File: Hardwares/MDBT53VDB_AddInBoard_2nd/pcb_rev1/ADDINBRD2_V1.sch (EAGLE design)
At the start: 11 parts, among them Q1 DMP2035UFDF-7, Q2 BC817-40QA, SW1 SKRPACE010, U1 SN74AHC1G00DRLR, U2 REF3325AIRSER

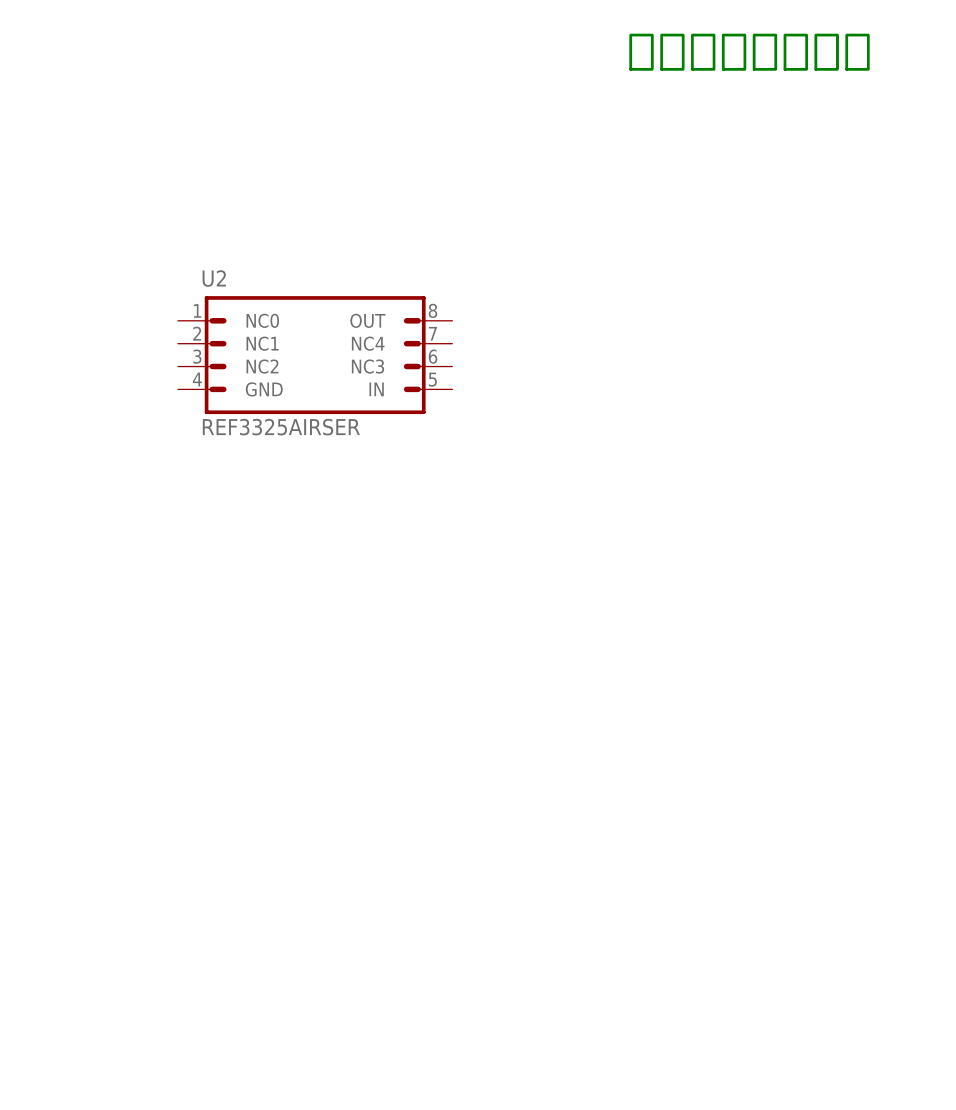
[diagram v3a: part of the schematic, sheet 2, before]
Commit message: 回路図を修正
・基準電圧回路にバイパスコンデンサーを配置
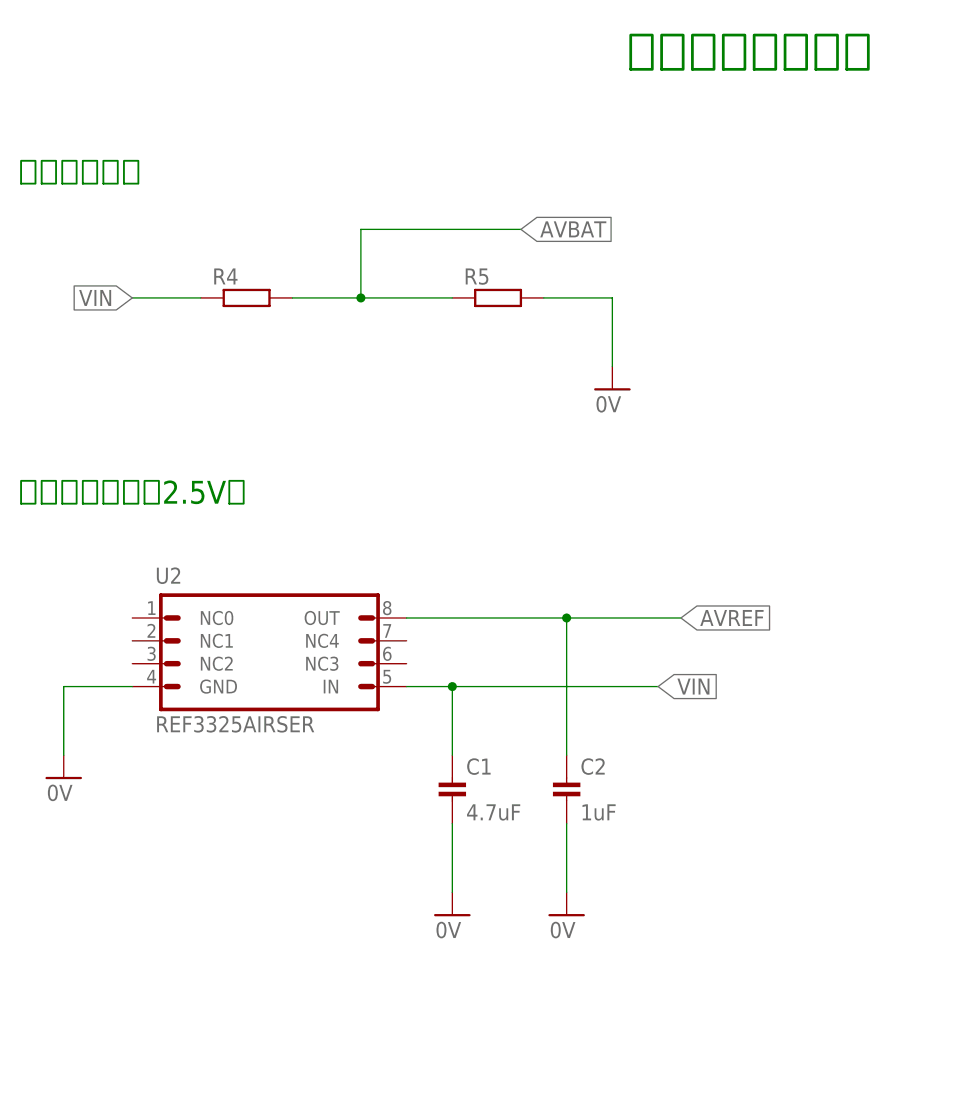
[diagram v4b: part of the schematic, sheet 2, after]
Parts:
- added C1: 4.7uF, SMDs:JMK105BBJ475MVHF
- added C2: 1uF, SMDs:GRM155R70J105KA12J
- added R4, R5: (no value), Parts:RESISTOR_0402N
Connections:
- new net AVBAT: R4.2, R5.1
- new net AVREF: C2.1, U2.OUT
- net 0V: now also C1.2, C2.2, R5.2, U2.GND
- net VIN: now also C1.1, R4.1, U2.IN
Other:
- note added: "基準電圧生成（2.5V）"
- note added: "電源電圧分圧"
- moved on the sheet: U2
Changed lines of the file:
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@@
 <part name="GND4" library="Supply" deviceset="0V" device=""/>
 <part name="U2" library="ICs" deviceset="REF33" device="25AIRSER"/>
+<part name="R4" library="Parts" deviceset="RESISTOR" device="_0402N"/>
+<part name="R5" library="Parts" deviceset="RESISTOR" device="_0402N"/>
+<part name="GND5" library="Supply" deviceset="0V" device=""/>
+<part name="GND6" library="Supply" deviceset="0V" device=""/>
+<part name="GND7" library="Supply" deviceset="0V" device=""/>
+<part name="GND8" library="Supply" deviceset="0V" device=""/>
+<part name="C1" library="SMDs" deviceset="JMK105BBJ" device="475MVHF" value="4.7uF"/>
+<part name="C2" library="SMDs" deviceset="GRM155" device="R70J105KA12J" value="1uF"/>
 </parts>
 <sheets>
@@
 for MDBT53V-DB</text>
 <text x="129.54" y="152.4" size="3.81" layer="91" align="bottom-center">電源電圧測定回路</text>
+<text x="48.26" y="142.24" size="2.54" layer="91" align="top-left">電源電圧分圧</text>
+<text x="48.26" y="106.68" size="2.54" layer="91" align="top-left">基準電圧生成（2.5V）</text>
 </plain>
 <instances>
 <instance part="FRAME2" gate="G$1" x="0" y="0"/>
-<instance part="U2" gate="G$1" x="81.28" y="119.38"/>
+<instance part="U2" gate="G$1" x="76.2" y="86.36"/>
+<instance part="R4" gate="G$1" x="68.58" y="127"/>
+<instance part="R5" gate="G$1" x="96.52" y="127"/>
+<instance part="GND5" gate="1" x="114.3" y="116.84"/>
+<instance part="GND6" gate="1" x="53.34" y="73.66"/>
+<instance part="GND7" gate="1" x="96.52" y="58.42"/>
+<instance part="GND8" gate="1" x="109.22" y="58.42"/>
+<instance part="C1" gate="G$1" x="96.52" y="76.2"/>
+<instance part="C2" gate="G$1" x="109.22" y="76.2"/>
 </instances>
 <busses>
 </busses>
 <nets>
+<net name="VIN" class="0">
+<segment>
+<pinref part="R4" gate="G$1" pin="1"/>
+<wire x1="68.58" y1="127" x2="60.96" y2="127" width="0.1524" layer="91"/>
+<label x="60.96" y="127" size="1.778" layer="95" rot="R180" xref="yes"/>
+</segment>
+<segment>
+<pinref part="U2" gate="G$1" pin="IN"/>
+<wire x1="91.44" y1="83.82" x2="96.52" y2="83.82" width="0.1524" layer="91"/>
+<label x="119.38" y="83.82" size="1.778" layer="95" xref="yes"/>
+<wire x1="96.52" y1="83.82" x2="119.38" y2="83.82" width="0.1524" layer="91"/>
+<junction x="96.52" y="83.82"/>
+<pinref part="C1" gate="G$1" pin="1"/>
+<wire x1="96.52" y1="83.82" x2="96.52" y2="76.2" width="0.1524" layer="91"/>
+</segment>
+</net>
+<net name="AVBAT" class="0">
+<segment>
+<pinref part="R4" gate="G$1" pin="2"/>
+<pinref part="R5" gate="G$1" pin="1"/>
+<wire x1="78.74" y1="127" x2="86.36" y2="127" width="0.1524" layer="91"/>
+<wire x1="86.36" y1="127" x2="96.52" y2="127" width="0.1524" layer="91"/>
+<wire x1="86.36" y1="127" x2="86.36" y2="134.62" width="0.1524" layer="91"/>
+<wire x1="86.36" y1="134.62" x2="104.14" y2="134.62" width="0.1524" layer="91"/>
+<junction x="86.36" y="127"/>
+<label x="104.14" y="134.62" size="1.778" layer="95" xref="yes"/>
+</segment>
+</net>
+<net name="0V" class="0">
+<segment>
+<pinref part="R5" gate="G$1" pin="2"/>
+<pinref part="GND5" gate="1" pin="0V"/>
+<wire x1="106.68" y1="127" x2="114.3" y2="127" width="0.1524" layer="91"/>
+<wire x1="114.3" y1="127" x2="114.3" y2="119.38" width="0.1524" layer="91"/>
+</segment>
+<segment>
+<pinref part="U2" gate="G$1" pin="GND"/>
+<pinref part="GND6" gate="1" pin="0V"/>
+<wire x1="60.96" y1="83.82" x2="53.34" y2="83.82" width="0.1524" layer="91"/>
+<wire x1="53.34" y1="83.82" x2="53.34" y2="76.2" width="0.1524" layer="91"/>
+</segment>
+<segment>
+<pinref part="C1" gate="G$1" pin="2"/>
+<pinref part="GND7" gate="1" pin="0V"/>
+<wire x1="96.52" y1="68.58" x2="96.52" y2="60.96" width="0.1524" layer="91"/>
+</segment>
+<segment>
+<pinref part="C2" gate="G$1" pin="2"/>
+<pinref part="GND8" gate="1" pin="0V"/>
+<wire x1="109.22" y1="68.58" x2="109.22" y2="60.96" width="0.1524" layer="91"/>
+</segment>
+</net>
+<net name="AVREF" class="0">
+<segment>
+<pinref part="U2" gate="G$1" pin="OUT"/>
+<wire x1="91.44" y1="91.44" x2="109.22" y2="91.44" width="0.1524" layer="91"/>
+<label x="121.92" y="91.44" size="1.778" layer="95" xref="yes"/>
+<wire x1="109.22" y1="91.44" x2="121.92" y2="91.44" width="0.1524" layer="91"/>
+<junction x="109.22" y="91.44"/>
+<pinref part="C2" gate="G$1" pin="1"/>
+<wire x1="109.22" y1="91.44" x2="109.22" y2="76.2" width="0.1524" layer="91"/>
+</segment>
+</net>
 </nets>
 </sheet>

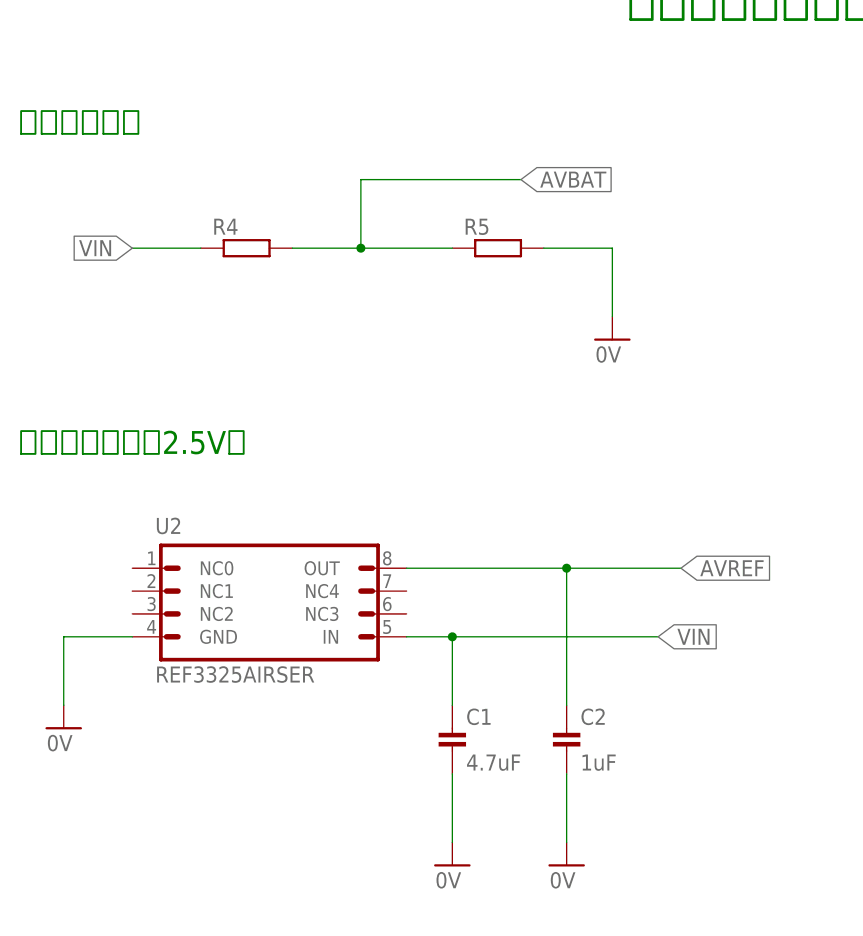
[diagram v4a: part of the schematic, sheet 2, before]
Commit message: 回路図を修正
・分圧回路を追加
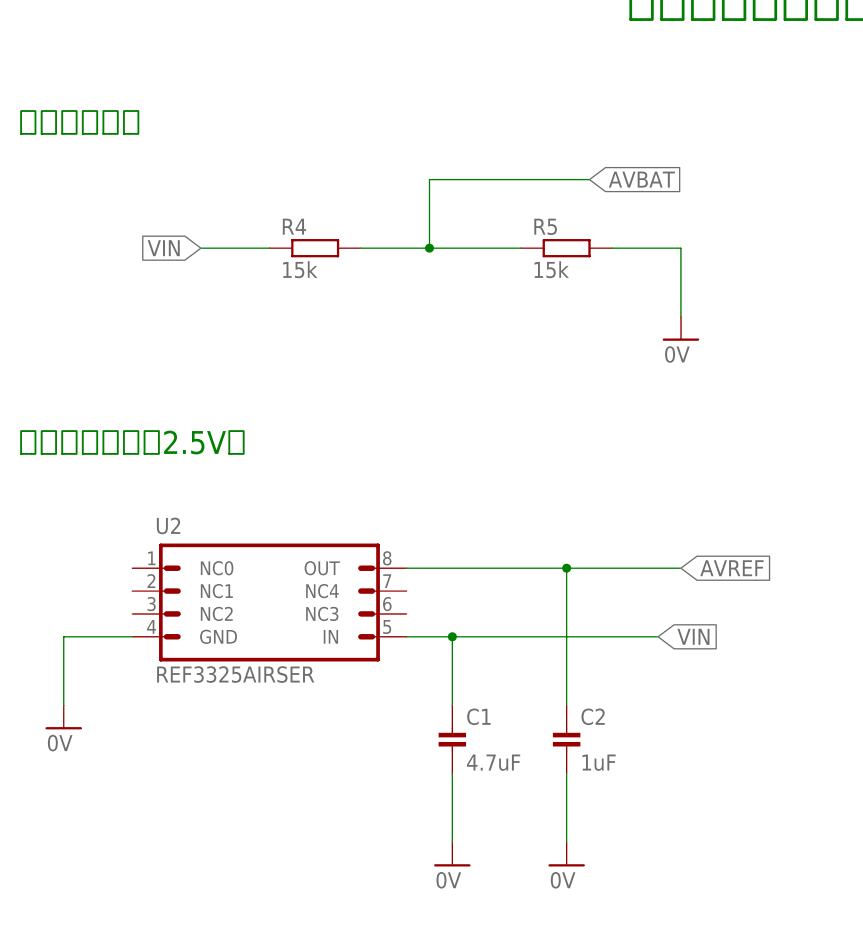
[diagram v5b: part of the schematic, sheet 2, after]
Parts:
- R4, R5: value (none) -> 15k; device Parts:RESISTOR_0402N -> SMDs:ERA-2APB153X
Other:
- moved on the sheet: R4, R5
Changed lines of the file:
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@@
 <part name="GND4" library="Supply" deviceset="0V" device=""/>
 <part name="U2" library="ICs" deviceset="REF33" device="25AIRSER"/>
-<part name="R4" library="Parts" deviceset="RESISTOR" device="_0402N"/>
-<part name="R5" library="Parts" deviceset="RESISTOR" device="_0402N"/>
 <part name="GND5" library="Supply" deviceset="0V" device=""/>
 <part name="GND6" library="Supply" deviceset="0V" device=""/>
@@
 <part name="C1" library="SMDs" deviceset="JMK105BBJ" device="475MVHF" value="4.7uF"/>
 <part name="C2" library="SMDs" deviceset="GRM155" device="R70J105KA12J" value="1uF"/>
+<part name="R4" library="SMDs" deviceset="ERA-2A" device="PB153X" value="15k"/>
+<part name="R5" library="SMDs" deviceset="ERA-2A" device="PB153X" value="15k"/>
 </parts>
 <sheets>
@@
 <instance part="FRAME2" gate="G$1" x="0" y="0"/>
 <instance part="U2" gate="G$1" x="76.2" y="86.36"/>
-<instance part="R4" gate="G$1" x="68.58" y="127"/>
-<instance part="R5" gate="G$1" x="96.52" y="127"/>
-<instance part="GND5" gate="1" x="114.3" y="116.84"/>
+<instance part="GND5" gate="1" x="121.92" y="116.84"/>
 <instance part="GND6" gate="1" x="53.34" y="73.66"/>
 <instance part="GND7" gate="1" x="96.52" y="58.42"/>
 <instance part="GND8" gate="1" x="109.22" y="58.42"/>
-<instance part="C1" gate="G$1" x="96.52" y="76.2"/>
-<instance part="C2" gate="G$1" x="109.22" y="76.2"/>
+<instance part="C1" gate="G$1" x="96.52" y="73.66"/>
+<instance part="C2" gate="G$1" x="109.22" y="73.66"/>
+<instance part="R4" gate="G$1" x="81.28" y="127"/>
+<instance part="R5" gate="G$1" x="109.22" y="127"/>
 </instances>
 <busses>
@@
 <net name="VIN" class="0">
 <segment>
+<wire x1="76.2" y1="127" x2="68.58" y2="127" width="0.1524" layer="91"/>
+<label x="68.58" y="127" size="1.778" layer="95" rot="R180" xref="yes"/>
 <pinref part="R4" gate="G$1" pin="1"/>
-<wire x1="68.58" y1="127" x2="60.96" y2="127" width="0.1524" layer="91"/>
-<label x="60.96" y="127" size="1.778" layer="95" rot="R180" xref="yes"/>
 </segment>
 <segment>
@@
 <net name="AVBAT" class="0">
 <segment>
+<wire x1="86.36" y1="127" x2="93.98" y2="127" width="0.1524" layer="91"/>
+<wire x1="93.98" y1="127" x2="104.14" y2="127" width="0.1524" layer="91"/>
+<wire x1="93.98" y1="127" x2="93.98" y2="134.62" width="0.1524" layer="91"/>
+<wire x1="93.98" y1="134.62" x2="111.76" y2="134.62" width="0.1524" layer="91"/>
+<junction x="93.98" y="127"/>
+<label x="111.76" y="134.62" size="1.778" layer="95" xref="yes"/>
 <pinref part="R4" gate="G$1" pin="2"/>
 <pinref part="R5" gate="G$1" pin="1"/>
-<wire x1="78.74" y1="127" x2="86.36" y2="127" width="0.1524" layer="91"/>
-<wire x1="86.36" y1="127" x2="96.52" y2="127" width="0.1524" layer="91"/>
-<wire x1="86.36" y1="127" x2="86.36" y2="134.62" width="0.1524" layer="91"/>
-<wire x1="86.36" y1="134.62" x2="104.14" y2="134.62" width="0.1524" layer="91"/>
-<junction x="86.36" y="127"/>
-<label x="104.14" y="134.62" size="1.778" layer="95" xref="yes"/>
 </segment>
 </net>
 <net name="0V" class="0">
 <segment>
+<pinref part="GND5" gate="1" pin="0V"/>
+<wire x1="114.3" y1="127" x2="121.92" y2="127" width="0.1524" layer="91"/>
+<wire x1="121.92" y1="127" x2="121.92" y2="119.38" width="0.1524" layer="91"/>
 <pinref part="R5" gate="G$1" pin="2"/>
-<pinref part="GND5" gate="1" pin="0V"/>
-<wire x1="106.68" y1="127" x2="114.3" y2="127" width="0.1524" layer="91"/>
-<wire x1="114.3" y1="127" x2="114.3" y2="119.38" width="0.1524" layer="91"/>
-</segment>
-<segment>
+</segment>
+<segment>

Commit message: レイアウトを修正
・シルクの位置を修正
・部品ライブラリーの一部を入れ替え
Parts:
- F1: device Parts:FCC16102ABTP -> SMDs:FCC16102ABTP
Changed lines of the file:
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@@
 <part name="FRAME1" library="Generic" deviceset="A4L-LOC" device=""/>
 <part name="FRAME2" library="Generic" deviceset="A4L-LOC" device=""/>
-<part name="F1" library="Parts" deviceset="FCC16" device="102ABTP"/>
+<part name="F1" library="SMDs" deviceset="FCC16" device="102ABTP"/>
 <part name="D1" library="Parts" deviceset="PMEG4010" device="AESBYL"/>
 <part name="SW1" library="Parts" deviceset="SKRPACE010" device=""/>

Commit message: レイアウトを修正
・部品ライブラリーの一部を入れ替え
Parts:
- R1, R2: device Parts:RESISTOR_0402N -> SMDs:CRCW04025K10FKEDC
- R3: device Parts:RESISTOR_0402N -> SMDs:CRCW040251K0FKEDC
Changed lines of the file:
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@@
 <part name="GND1" library="Supply" deviceset="0V" device=""/>
 <part name="GND2" library="Supply" deviceset="0V" device=""/>
-<part name="R1" library="Parts" deviceset="RESISTOR" device="_0402N" value="5.1k"/>
+<part name="R1" library="SMDs" deviceset="CRCW0402" device="5K10FKEDC" value="5.1k"/>
 <part name="D2" library="Parts" deviceset="PMEG4010" device="AESBYL"/>
 <part name="Q1" library="Parts" deviceset="DMP2035" device="UFDF-7"/>
@@
 <part name="Q2" library="Parts" deviceset="BC817" device="-40QA"/>
 <part name="GND3" library="Supply" deviceset="0V" device=""/>
-<part name="R2" library="Parts" deviceset="RESISTOR" device="_0402N" value="5.1k"/>
-<part name="R3" library="Parts" deviceset="RESISTOR" device="_0402N" value="51k"/>
+<part name="R2" library="SMDs" deviceset="CRCW0402" device="5K10FKEDC" value="5.1k"/>
+<part name="R3" library="SMDs" deviceset="CRCW0402" device="51K0FKEDC" value="51k"/>
 <part name="GND4" library="Supply" deviceset="0V" device=""/>
 <part name="U2" library="ICs" deviceset="REF33" device="25AIRSER"/>
@@
 <instance part="GND1" gate="1" x="116.84" y="116.84"/>
 <instance part="GND2" gate="1" x="132.08" y="88.9"/>
-<instance part="R1" gate="G$1" x="132.08" y="121.92" rot="R90"/>
+<instance part="R1" gate="G$1" x="132.08" y="127" rot="R90"/>
 <instance part="D2" gate="G$1" x="170.18" y="137.16" smashed="yes">
 <attribute name="NAME" x="162.56" y="132.08" size="1.778" layer="95"/>
@@
 <instance part="Q2" gate="G$1" x="162.56" y="63.5"/>
 <instance part="GND3" gate="1" x="101.6" y="50.8"/>
-<instance part="R2" gate="G$1" x="142.24" y="63.5"/>
-<instance part="R3" gate="G$1" x="157.48" y="48.26" rot="R90"/>
+<instance part="R2" gate="G$1" x="147.32" y="63.5"/>
+<instance part="R3" gate="G$1" x="157.48" y="53.34" rot="R90"/>
 <instance part="GND4" gate="1" x="167.64" y="35.56"/>
 </instances>
@@
 <pinref part="F1" gate="G$1" pin="2"/>
 <wire x1="99.06" y1="137.16" x2="116.84" y2="137.16" width="0.1524" layer="91"/>
-<pinref part="R1" gate="G$1" pin="2"/>
 <wire x1="116.84" y1="137.16" x2="132.08" y2="137.16" width="0.1524" layer="91"/>
-<wire x1="132.08" y1="137.16" x2="132.08" y2="132.08" width="0.1524" layer="91"/>
 <pinref part="D1" gate="G$1" pin="C"/>
 <wire x1="116.84" y1="137.16" x2="116.84" y2="129.54" width="0.1524" layer="91"/>
@@
 <pinref part="Q1" gate="G$1" pin="S"/>
 <wire x1="132.08" y1="137.16" x2="147.32" y2="137.16" width="0.1524" layer="91"/>
+<pinref part="R1" gate="G$1" pin="2"/>
+<wire x1="132.08" y1="132.08" x2="132.08" y2="137.16" width="0.1524" layer="91"/>
 </segment>
 </net>
@@
 <pinref part="GND4" gate="1" pin="0V"/>
 <wire x1="167.64" y1="58.42" x2="167.64" y2="43.18" width="0.1524" layer="91"/>
+<wire x1="167.64" y1="43.18" x2="167.64" y2="38.1" width="0.1524" layer="91"/>
+<junction x="167.64" y="43.18"/>
 <pinref part="R3" gate="G$1" pin="1"/>
-<wire x1="167.64" y1="43.18" x2="167.64" y2="38.1" width="0.1524" layer="91"/>
 <wire x1="157.48" y1="48.26" x2="157.48" y2="43.18" width="0.1524" layer="91"/>
 <wire x1="157.48" y1="43.18" x2="167.64" y2="43.18" width="0.1524" layer="91"/>
-<junction x="167.64" y="43.18"/>
 </segment>
 </net>
 <net name="PWR_G" class="0">
 <segment>
-<pinref part="R1" gate="G$1" pin="1"/>
 <pinref part="SW1" gate="G$1" pin="S"/>
-<wire x1="132.08" y1="121.92" x2="132.08" y2="116.84" width="0.1524" layer="91"/>
 <pinref part="SW1" gate="G$1" pin="S1"/>
 <wire x1="132.08" y1="116.84" x2="132.08" y2="111.76" width="0.1524" layer="91"/>
@@
 <junction x="149.86" y="116.84"/>
 <junction x="132.08" y="111.76"/>
+<pinref part="R1" gate="G$1" pin="1"/>
+<wire x1="132.08" y1="121.92" x2="132.08" y2="116.84" width="0.1524" layer="91"/>
 </segment>
 <segment>
@@
 </segment>
 </net>
-<net name="N$2" class="0">
-<segment>
-<pinref part="U1" gate="G$1" pin="Y"/>
-<pinref part="R2" gate="G$1" pin="1"/>
-<wire x1="134.62" y1="63.5" x2="142.24" y2="63.5" width="0.1524" layer="91"/>
-</segment>
-</net>
 <net name="N$5" class="0">
 <segment>
+<pinref part="Q2" gate="G$1" pin="B"/>
+<wire x1="157.48" y1="63.5" x2="162.56" y2="63.5" width="0.1524" layer="91"/>
+<junction x="157.48" y="63.5"/>
 <pinref part="R2" gate="G$1" pin="2"/>
-<pinref part="Q2" gate="G$1" pin="B"/>
 <wire x1="152.4" y1="63.5" x2="157.48" y2="63.5" width="0.1524" layer="91"/>
 <pinref part="R3" gate="G$1" pin="2"/>
-<wire x1="157.48" y1="63.5" x2="162.56" y2="63.5" width="0.1524" layer="91"/>
 <wire x1="157.48" y1="58.42" x2="157.48" y2="63.5" width="0.1524" layer="91"/>
-<junction x="157.48" y="63.5"/>
-</segment>
-</net>
+</segment>
+</net>
+<net name="N$3" class="0">
+<segment>
+<pinref part="R2" gate="G$1" pin="1"/>
+<pinref part="U1" gate="G$1" pin="Y"/>
+<wire x1="142.24" y1="63.5" x2="134.62" y2="63.5" width="0.1524" layer="91"/>
+</segment>
+</net>

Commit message: レイアウトを修正
・部品ライブラリーの一部を入れ替え
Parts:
- D1, D2: device Parts:PMEG4010AESBYL -> SMDs:PMEG4010AESBYL
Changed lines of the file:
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@@
 <part name="FRAME2" library="Generic" deviceset="A4L-LOC" device=""/>
 <part name="F1" library="SMDs" deviceset="FCC16" device="102ABTP"/>
-<part name="D1" library="Parts" deviceset="PMEG4010" device="AESBYL"/>
+<part name="D1" library="SMDs" deviceset="PMEG4010" device="AESBYL"/>
 <part name="SW1" library="Parts" deviceset="SKRPACE010" device=""/>
 <part name="GND1" library="Supply" deviceset="0V" device=""/>
 <part name="GND2" library="Supply" deviceset="0V" device=""/>
 <part name="R1" library="SMDs" deviceset="CRCW0402" device="5K10FKEDC" value="5.1k"/>
-<part name="D2" library="Parts" deviceset="PMEG4010" device="AESBYL"/>
+<part name="D2" library="SMDs" deviceset="PMEG4010" device="AESBYL"/>
 <part name="Q1" library="Parts" deviceset="DMP2035" device="UFDF-7"/>
 <part name="U1" library="Parts" deviceset="SN74AHC1G00" device="DRLR"/>
